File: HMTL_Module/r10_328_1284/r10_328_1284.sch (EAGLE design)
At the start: 40 parts, among them J2 AVR_SPI_PRG_6PTH, U2 ATMEGA328P_PDIP, Y1 20MHz

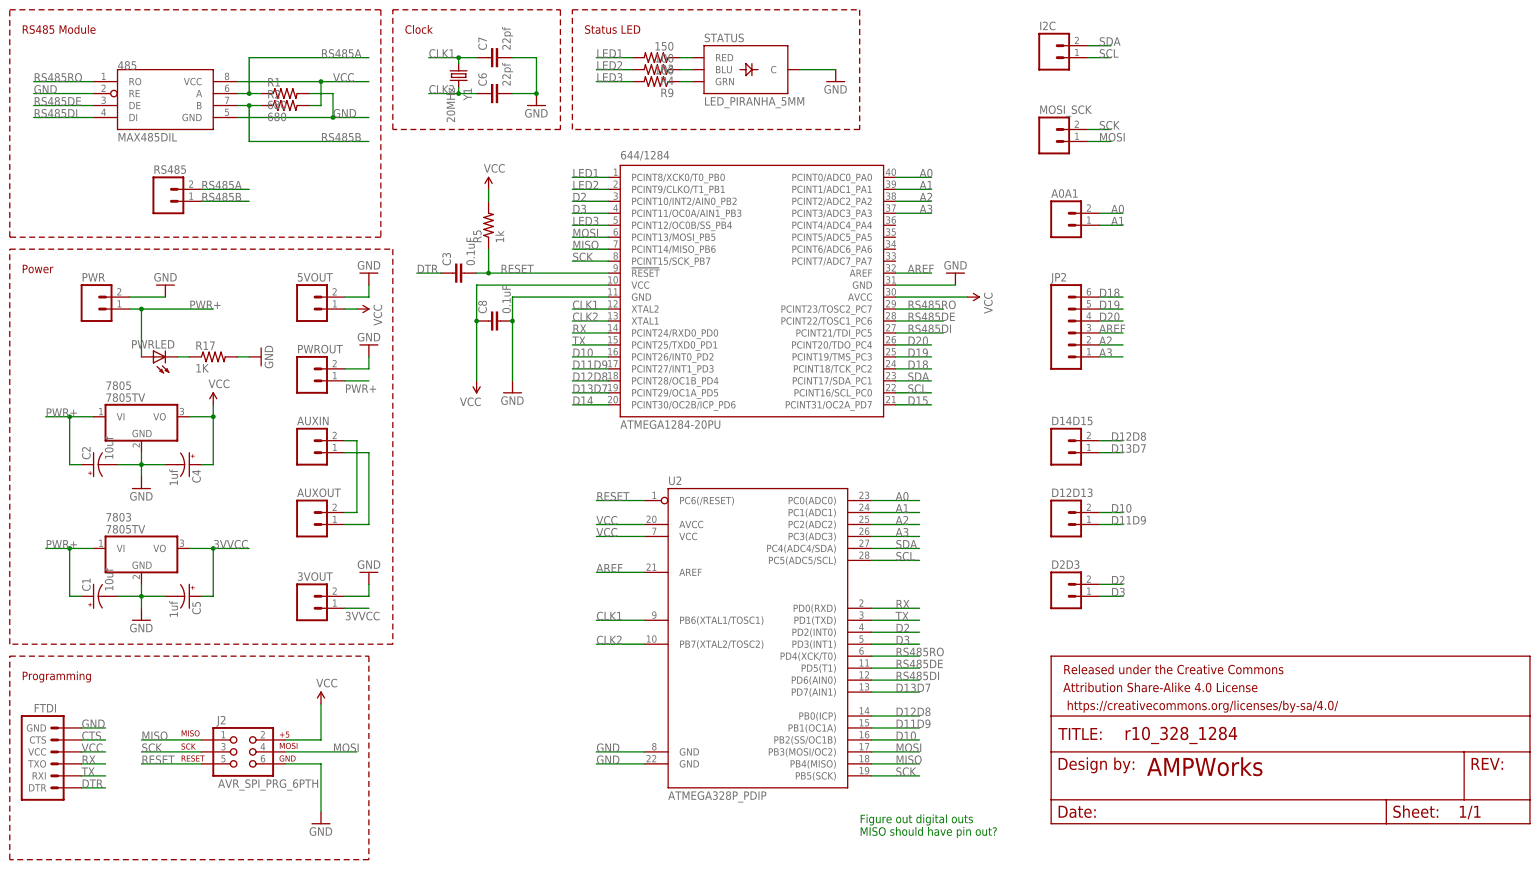
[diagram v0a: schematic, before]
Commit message: For HTML 328/1284 module added LED for 328
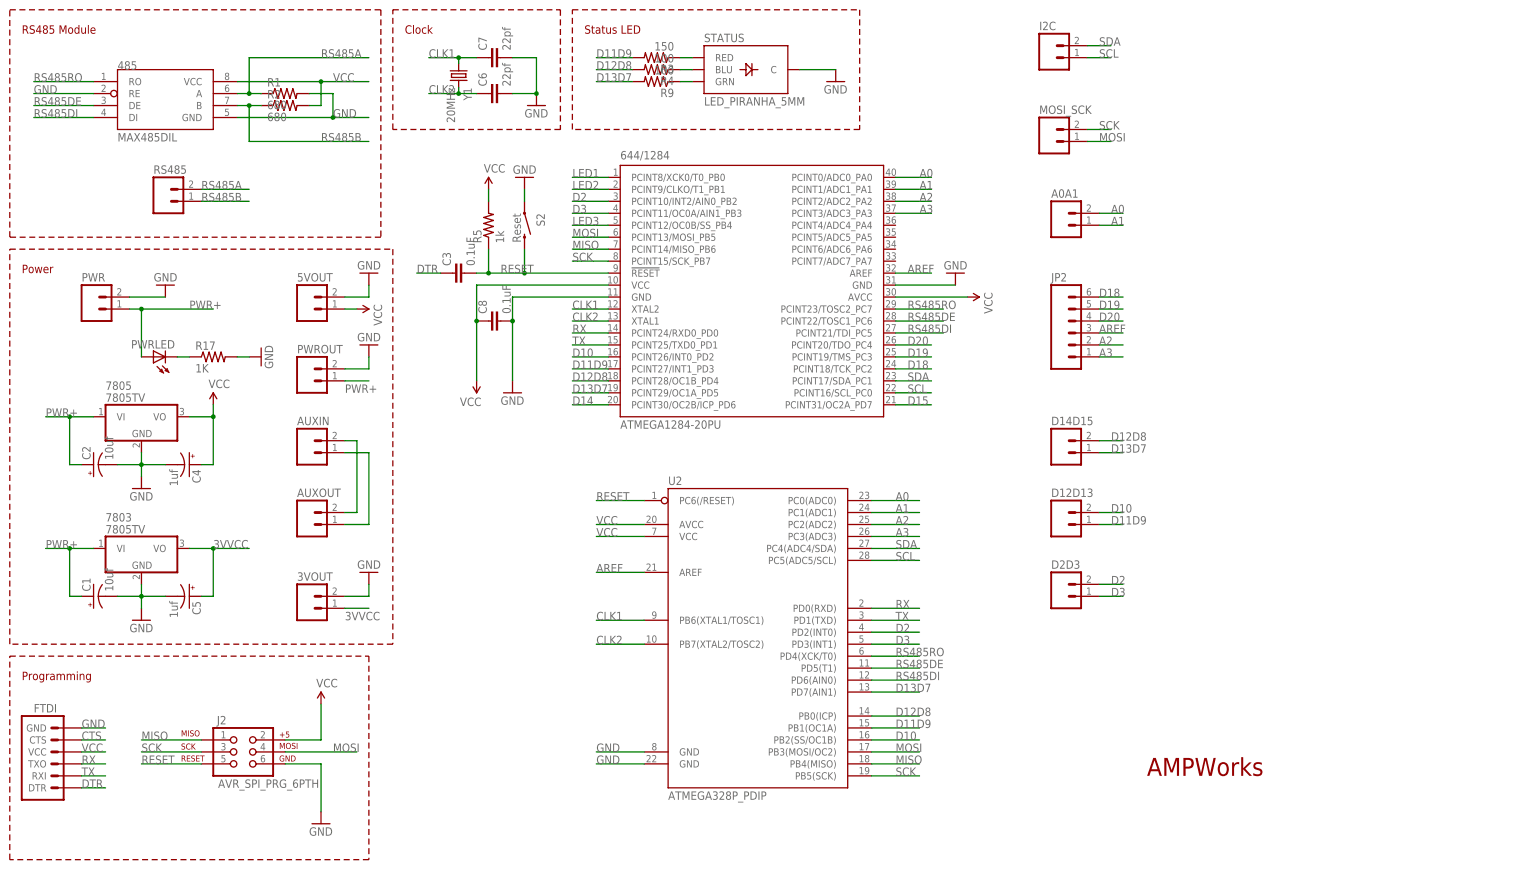
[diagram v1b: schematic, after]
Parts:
- removed FRAME1: FRAME-LETTER, SparkFun-Aesthetics:FRAME-LETTER
- added S2: Reset, SparkFun:SWITCH-MOMENTARY-2SMD
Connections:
- net D11D9: now also R3.2
- net D12D8: now also R4.2
- net D13D7: now also R9.2
- net GND: now also S2.1
- net LED1: no longer R3.2
- net LED2: no longer R4.2
- net LED3: no longer R9.2
- net RESET: now also S2.2
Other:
- note removed: "Figure out digital outs MISO should have pin out?"
